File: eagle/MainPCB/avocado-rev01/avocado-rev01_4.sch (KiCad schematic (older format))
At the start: 2 parts, among them U1 V3S

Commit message: decoupling caps
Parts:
- added C22, C23, C24, C25, C26, C27, C28, C29, C30, C31, C32, C33, C34, C35, C36, C37, C38, C40, C41, C42, C43, C44: 10u, avocado-rev01:C0603, symbol avocado-rev01-eagle-import:C0603
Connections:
- net 1V2: now also C32.1, C34.1, C35.1, C36.1, C37.1, C38.1, C40.1, C41.1, C42.1
- net 1V8: now also C29.1, C30.1, C31.1, C33.1
- net 3V3: now also C22.1, C23.1, C24.1, C25.1, C26.1, C27.1, C28.1, C43.1, C44.1
- net GND: now also C22.2, C23.2, C24.2, C25.2, C26.2, C27.2, C28.2, C29.2, C30.2, C31.2, C32.2, C33.2, C34.2, C35.2, C36.2, C37.2, C38.2, C40.2, C41.2, C42.2, C43.2, C44.2

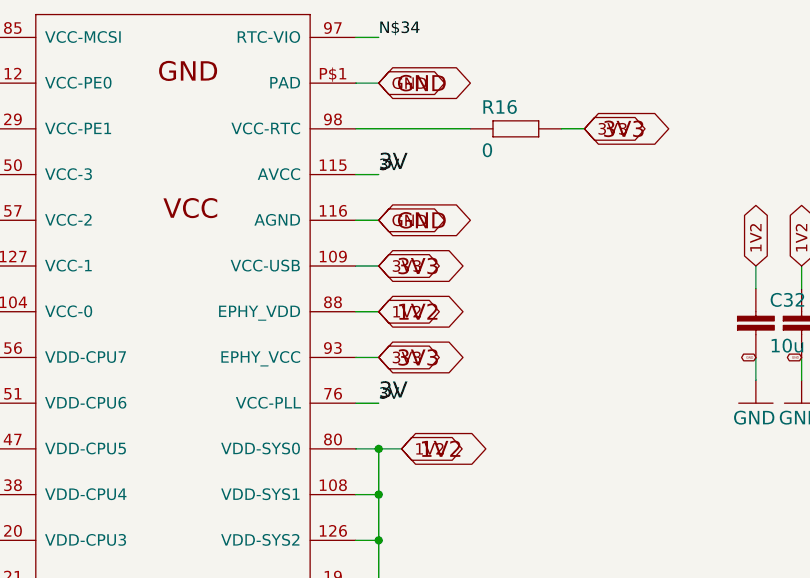
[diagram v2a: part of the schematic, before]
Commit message: added 3V rail
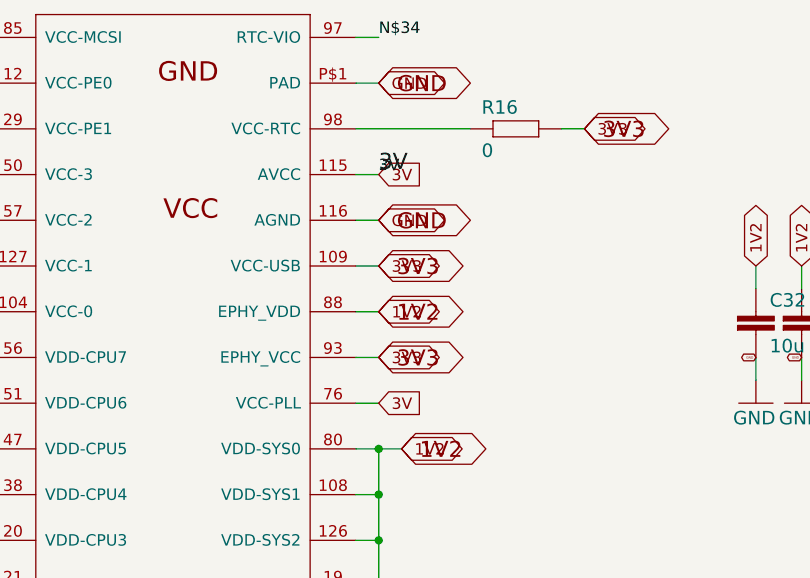
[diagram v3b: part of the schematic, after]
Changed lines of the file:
@@
 Wire Wire Line
 	4900 2500 5000 2500
-Text Label 5000 2500 0    50   ~ 0
-3V
-Text Label 5000 2500 0    70   ~ 0
-3V
 Wire Wire Line
 	4900 1500 5000 1500
@@
 Wire Wire Line
 	8250 2300 8250 2400
+Text GLabel 5000 2500 2    50   Input ~ 0
+3V
+Text GLabel 5000 1500 2    50   Input ~ 0
+3V
 $EndSCHEMATC
